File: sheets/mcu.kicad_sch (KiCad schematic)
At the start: 52 parts, among them J4 SWD, J5 Qwiic, J6 Fan, J7 Spare, Q33 DMG3415U-7, Q34 2N7002, Q35 2N7002, SW1 DIP-4, SW2 LED_KILL, SW3 BOOTSEL, SW4 RUN, U24 RP2040, U25 W25Q128JVS, U26 TMP112AIDRLR, U27 TMP112AIDRLR, U28 SK6805-EC15, Y1 12MHz

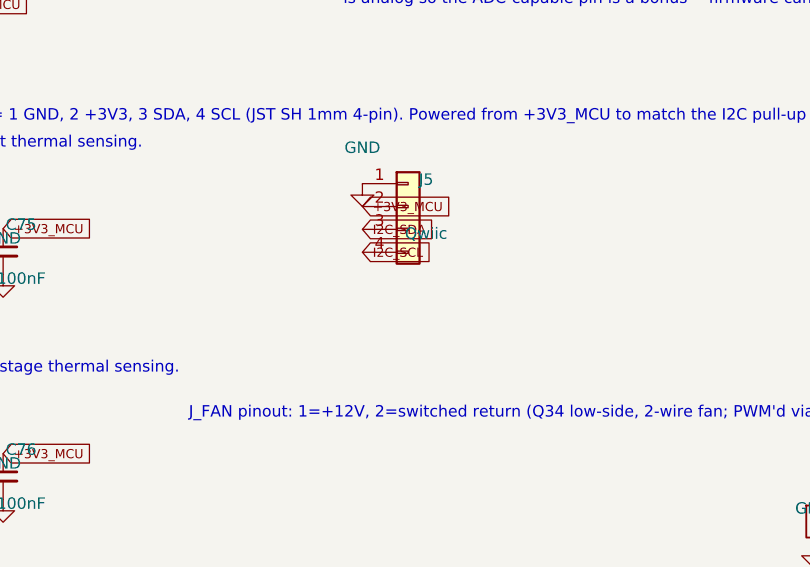
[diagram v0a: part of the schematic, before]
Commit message: sch: resolve all footprint-pad/symbol-pin mismatches from GUI import log
Q20/Q22/Q23: stacked hidden S pins (2,3) added to Q_NMOS_TDSON_PQFN,
matching KiCad's own stock Q_NMOS_SSSGD_AvalancheRated convention, so
TDSON-8-1/PQFN-8-EP's separately-numbered source pads all bind.

U22 (TL431 SOT-23-5): verified against TI's real datasheet (SLVS543S) --
the existing pin binding (K=3/REF=4/A=5) was already correct; pads 1/2 are
datasheet-documented NC/substrate pins, allowlisted rather than rewired.

U13/U14 (INA226): swapped the wrong EP-bearing HVSSOP-10 footprint for the
real no-EP VSSOP-10/MSOP-10 JEDEC MO-187 footprint per TI's SBOS547B
mechanical drawing; removed the now-incorrect EP-VIA property.

J5 (Qwiic JST-SH): switched to KiCad's stock Conn_01x04_MountingPin symbol
pairing convention, added a passive un-grounded MP pin + no-connect flag.

tools/check_footprints.py: added the reverse pad-to-pin coverage check
(catches all of the above) with a documented, datasheet-cited allowlist
for the 3 legitimately-unmapped pads (U22 x2, U30 x1) and stale-entry
detection.

Verification: check_nets.py and check_footprints.py (extended) both pass;
ERC 0 errors / 652 warnings (identical category breakdown to Task-14
baseline); netlist export clean, 363 components / 334 nets unchanged;
net-to-electrode mapping proof table in task-15-report.md confirms zero
connectivity changes beyond the explicitly-authorized additions.

Co-Authored-By: Claude Fable 5 <noreply@anthropic.com>
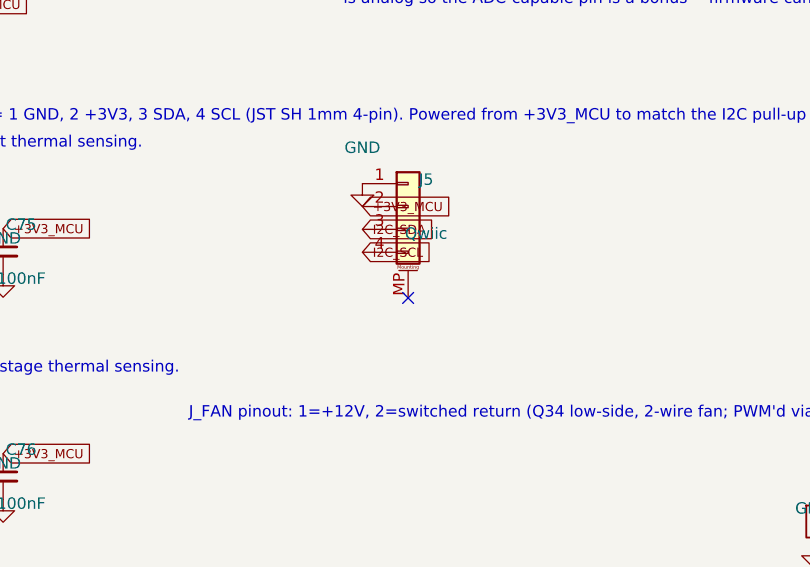
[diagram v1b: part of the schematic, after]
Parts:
- J5: symbol Connector_Generic:Conn_01x04 -> Connector_Generic_MountingPin:Conn_01x04_MountingPin
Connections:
- no-connect marks 4 -> 5
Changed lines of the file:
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@@
 	)
 	(symbol
-		(lib_id "Connector_Generic:Conn_01x04")
+		(lib_id "Connector_Generic_MountingPin:Conn_01x04_MountingPin")
 		(at 300 55 0)
 		(unit 1)
@@
 		(pin "3")
 		(pin "4")
+		(pin "MP")
 		(instances
 			(project "sierra-to-usb"
@@
 		)
 	)
+	(no_connect
+		(at 300 65.16)
+	)
 	(symbol
